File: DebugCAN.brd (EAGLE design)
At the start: 64 x 57 mm, 56 parts, among them J1 8P8C-LED, J2 MICRO-USB-RECEPTACLE47589-0001, J3 MA04-1, J5 8P8C-LED, J6 8P8C-LED, J7 8P8C-LED, U1 STM32F302C, U2 NCV7351D1E, U3 SI8621AB-B-IS, U4 AP2127N-3.3TRG1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

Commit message: 微修正
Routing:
- net GNDIO: track 201.0 -> 198.6 mm
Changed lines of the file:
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@@
 <wire x1="42" y1="28.75" x2="41.82" y2="28.723" width="0.1524" layer="1"/>
 <wire x1="42" y1="31.25" x2="41.82" y2="31.39" width="0.1524" layer="1"/>
-<wire x1="38.25" y1="23" x2="41.5" y2="19.75" width="0.1524" layer="1"/>
-<wire x1="38.25" y1="26" x2="38.25" y2="23" width="0.1524" layer="1"/>
-<wire x1="39.5" y1="26" x2="38.25" y2="26" width="0.1524" layer="1"/>
-<wire x1="42" y1="28.5" x2="39.5" y2="26" width="0.1524" layer="1"/>
+<wire x1="40.25" y1="21" x2="41.5" y2="19.75" width="0.1524" layer="1"/>
+<wire x1="40.25" y1="26.75" x2="40.25" y2="21" width="0.1524" layer="1"/>
+<wire x1="42" y1="28.5" x2="40.25" y2="26.75" width="0.1524" layer="1"/>
 <wire x1="41.5" y1="19.75" x2="41.71" y2="19.75" width="0.1524" layer="1"/>
 <wire x1="42" y1="28.5" x2="41.82" y2="28.723" width="0.1524" layer="1"/>
@@
 <wire x1="11.71" y1="17.46" x2="6.69" y2="17.46" width="0.5" layer="16"/>
 <wire x1="4.69" y1="15.46" x2="6.69" y2="17.46" width="0.5" layer="16"/>
-<wire x1="37.75" y1="26.25" x2="37.75" y2="17.5" width="0.5" layer="1"/>
-<wire x1="40" y1="28.5" x2="37.75" y2="26.25" width="0.5" layer="1"/>
+<wire x1="38.75" y1="27.25" x2="38.75" y2="18.5" width="0.5" layer="1"/>
+<wire x1="38.75" y1="18.5" x2="37.75" y2="17.5" width="0.5" layer="1"/>
+<wire x1="40" y1="28.5" x2="38.75" y2="27.25" width="0.5" layer="1"/>
 <wire x1="40" y1="28.5" x2="40.321" y2="28.469" width="0.5" layer="1"/>
 <wire x1="46.5" y1="48.75" x2="46.75" y2="48.5" width="0.5" layer="16"/>
@@
 <wire x1="28.11" y1="22.965" x2="26.26" y2="22.965" width="0.1524" layer="1"/>
 <wire x1="11.75" y1="23.875" x2="11.75" y2="22.25" width="0.1524" layer="1"/>
-<wire x1="11.75" y1="22.375" x2="11.75" y2="20.75" width="0.1524" layer="1"/>
-<wire x1="11.75" y1="20.75" x2="11.76" y2="20.68" width="0.1524" layer="1"/>
 <wire x1="11.75" y1="23.875" x2="11.37" y2="23.875" width="0.1524" layer="1"/>
 <wire x1="26.26" y1="22.965" x2="25.545" y2="22.25" width="0.1524" layer="1"/>
@@
 <vertex x="35.75" y="57"/>
 </polygon>
+<wire x1="11.75" y1="22.25" x2="11.76" y2="22.24" width="0.1524" layer="1"/>
+<wire x1="11.76" y1="22.24" x2="11.76" y2="20.68" width="0.1524" layer="1"/>
 </signal>
 <signal name="N$9">

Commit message: 最終調整(シルク)
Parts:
- moved R6 2.00 mm to (8.47, 43.0), turned to 180 degrees
- moved R7 2.00 mm to (8.54, 40.9), turned to 180 degrees
- moved R8 2.00 mm to (8.47, 38.7), turned to 180 degrees
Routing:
- net LED2: track 15.9 -> 11.3 mm
- net LED0: track 18.0 -> 13.4 mm
- net LED1: track 16.7 -> 12.3 mm
- net N$21: track 4.39 -> 3.86 mm
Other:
- board text added: "+3V3"
- board text added: "DebugCAN"
- board text added: "GND"
- board text added: "SWCLK"
- board text added: "SWDIO"
- board text added: "by ykc"

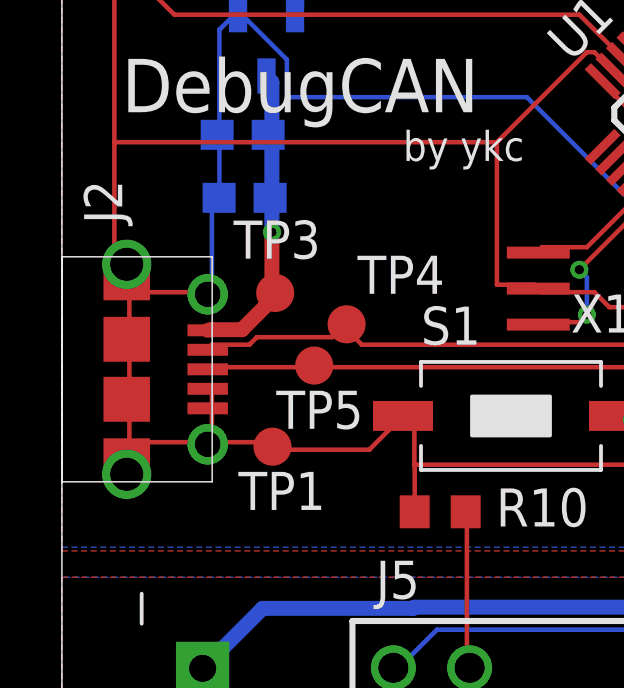
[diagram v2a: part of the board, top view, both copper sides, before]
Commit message: USBの変更
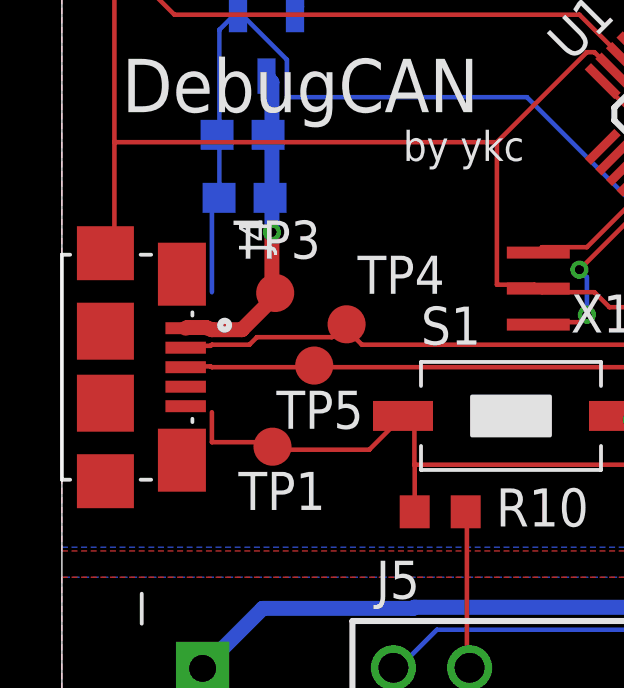
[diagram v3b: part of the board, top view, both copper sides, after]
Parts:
- removed J2: MICRO-USB-RECEPTACLE47589-0001, con-molex-usb:47589-0001
- added J4: 10118192-0001LF, con-usb:AMPHENOL_10118192-0001LF
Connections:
- net +5V: now also J4.1; no longer J2.1
- net GNDA: now also J4.4, J4.5, J4.SH1, J4.SH2, J4.SH3, J4.SH4, J4.SH5, J4.SH6; no longer J2.4, J2.5, J2.CASING1, J2.CASING2, J2.CASING3, J2.CASING4, J2.P$1, J2.P$2, J2.P$3, J2.P$4
- net USB_DM: now also J4.2; no longer J2.2
- net USB_DP: now also J4.3; no longer J2.3
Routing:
- net GNDA: track 217.4 -> 201.9 mm
- net +5V: track 10.4 -> 11.1 mm
- net USB_DP: track 35.9 -> 36.7 mm
- net USB_DM: track 49.7 -> 50.4 mm

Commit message: 微修正
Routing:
- net GNDA: track 201.9 -> 197.6 mm
- net +12V: track 105.5 -> 106.3 mm
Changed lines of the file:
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@@
 <drawing>
 <settings>
-<setting alwaysvectorfont="yes"/>
+<setting alwaysvectorfont="no"/>
 <setting verticaltext="up"/>
 </settings>
@@
 <wire x1="53.5" y1="19.5" x2="53.28" y2="19.65" width="0.5" layer="1"/>
 <wire x1="55" y1="18.75" x2="55.06" y2="18.63" width="0.5" layer="1"/>
-<wire x1="43.25" y1="25.25" x2="43.25" y2="28.25" width="0.5" layer="1"/>
-<wire x1="41.75" y1="25.25" x2="43.25" y2="25.25" width="0.5" layer="1"/>
-<wire x1="43.25" y1="28.25" x2="43.319" y2="28.469" width="0.5" layer="1"/>
 <wire x1="41.75" y1="25.25" x2="41.71" y2="25.15" width="0.5" layer="1"/>
 <wire x1="46.75" y1="25.25" x2="48.25" y2="23.75" width="0.5" layer="1"/>
-<wire x1="43.25" y1="25.25" x2="46.75" y2="25.25" width="0.5" layer="1"/>
+<wire x1="41.75" y1="25.25" x2="46.75" y2="25.25" width="0.5" layer="1"/>
 <wire x1="48.25" y1="23.75" x2="48.47" y2="23.64" width="0.5" layer="1"/>
 <wire x1="49.5" y1="23.5" x2="53.25" y2="19.75" width="0.5" layer="1"/>
@@
 <wire x1="41.75" y1="15.5" x2="41.64" y2="15.48" width="0.5" layer="16"/>
 <via x="37.75" y="14.25" extent="1-16" drill="0.3048"/>
+<wire x1="41.71" y1="25.15" x2="43.319" y2="26.759" width="0.5" layer="1"/>
+<wire x1="43.319" y1="26.759" x2="43.319" y2="28.469" width="0.5" layer="1"/>
 </signal>
 <signal name="+5V_ISO" class="1">
@@
 <wire x1="5.25" y1="33" x2="5.175" y2="33.245" width="0.1524" layer="16"/>
 <wire x1="5.25" y1="31.25" x2="5.24" y2="31.145" width="0.1524" layer="16"/>
-<wire x1="5" y1="28" x2="5" y2="31" width="0.1524" layer="16"/>
 <wire x1="5" y1="31" x2="5.24" y2="31.145" width="0.1524" layer="16"/>
 <wire x1="5.25" y1="36.75" x2="5.75" y2="37.25" width="0.1524" layer="16"/>
@@
 <wire x1="5" y1="23" x2="7" y2="23" width="0.1524" layer="1"/>
 <wire x1="7" y1="23" x2="7.02" y2="22.85" width="0.1524" layer="1"/>
-<wire x1="5" y1="23" x2="5" y2="24" width="0.1524" layer="1"/>
 <wire x1="1.75" y1="40.79" x2="1.75" y2="38.71" width="0.1524" layer="1"/>
 <wire x1="1.75" y1="40.79" x2="1.75" y2="42.87" width="0.1524" layer="1"/>
 <wire x1="1.75" y1="29" x2="1.75" y2="33" width="0.1524" layer="1"/>
 <wire x1="1.75" y1="33" x2="1.75" y2="38.71" width="0.1524" layer="1"/>
-<wire x1="2" y1="29" x2="1.75" y2="29" width="0.1524" layer="1"/>
 <wire x1="11.37" y1="23.875" x2="10.245" y2="22.75" width="0.1524" layer="1"/>
 <wire x1="10.245" y1="22.75" x2="7.25" y2="22.75" width="0.1524" layer="1"/>
